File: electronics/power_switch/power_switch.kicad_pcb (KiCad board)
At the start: 2 copper layers, 80 x 85 mm, 26 parts, among them CON1 AVR-ISP-6, IC1 ATTINY84-P, K1 WALLPLUG_NOEARTH_220V, K2 WALLSOCKET_NOEARTH_220V, P1 CONN_01X02, P2 5V=, P3 CONN_01X01, P4 CONN_01X01, Q1 BC548, Q2 BC548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

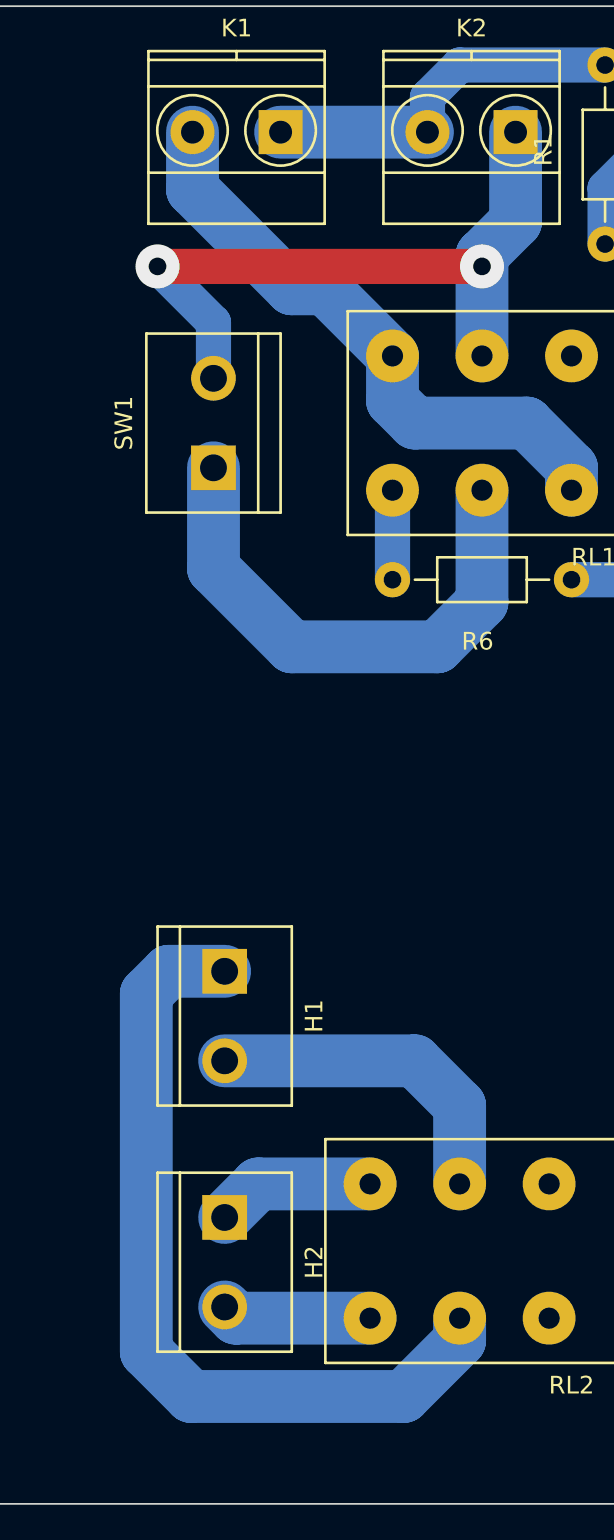
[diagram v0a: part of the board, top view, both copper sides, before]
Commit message: changed screw terminal
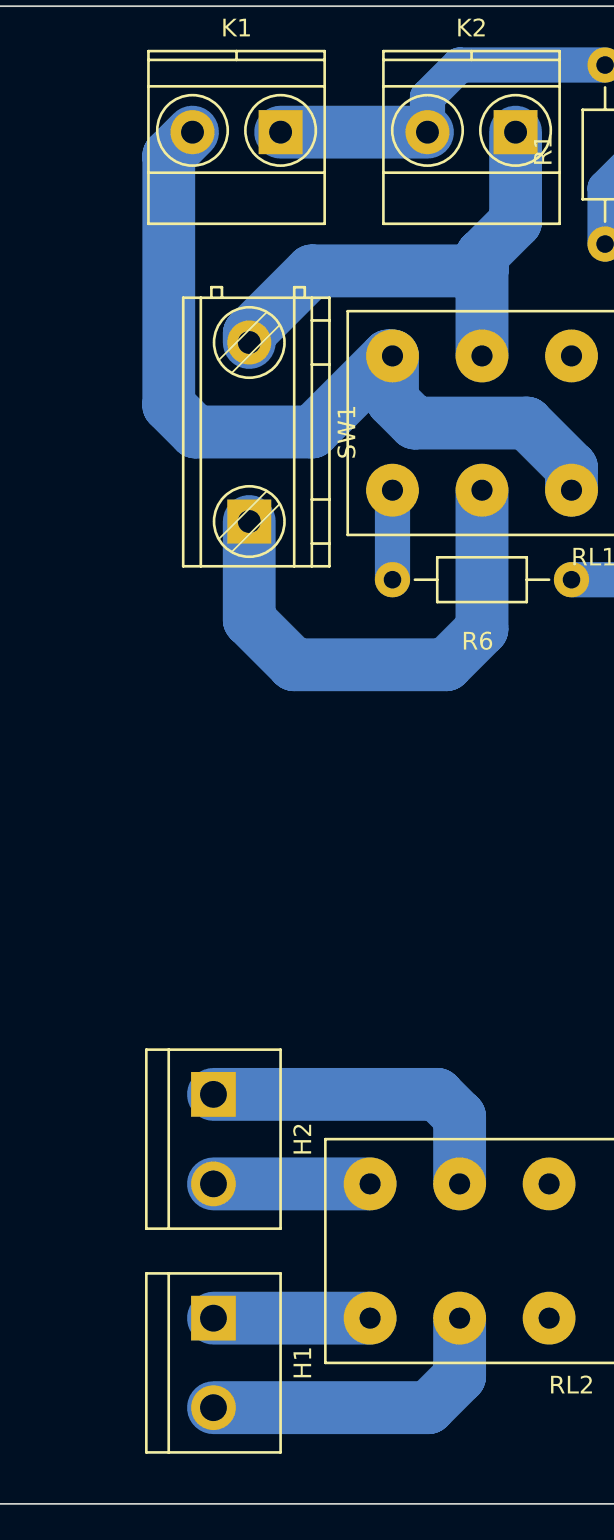
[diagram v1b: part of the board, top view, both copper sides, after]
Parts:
- SW1: footprint Connect:bornier2 -> special_symbols:TerminalBlock_RND-205-00243_RM10.16mm_2pol
- moved H1 19.7 mm to (53.3, 127.0)
- moved H2 7.01 mm to (53.3, 114.3)
- moved SW1 5.95 mm to (55.4, 79.2)
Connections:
- RL2 pad 11: Net-(H1-Pad1) -> Net-(H1-Pad2)
- RL2 pad 14: Net-(H2-Pad2) -> Net-(H1-Pad1)
- RL2 pad 21: Net-(H1-Pad2) -> Net-(H2-Pad1)
- RL2 pad 24: Net-(H2-Pad1) -> Net-(H2-Pad2)
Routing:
- net Net-(H1-Pad1): track 46.7 -> 8.89 mm
- net Net-(K1-Pad2): track 34.1 -> 46.7 mm
- net Net-(K2-Pad1): track 40.2 -> 29.6 mm, vias 2 -> 0
- net Net-(H2-Pad1): track 9.04 -> 18.3 mm
- net Net-(RL1-Pad11): track 30.2 -> 28.6 mm
- net Net-(H1-Pad2): track 18.8 -> 18.0 mm
